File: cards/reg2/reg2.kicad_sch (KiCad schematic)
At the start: 161 parts, among them J1 BUS, Q1 2N7000, Q10 2N7000, Q11 2N7000, Q12 2N7000, Q13 2N7000, Q14 2N7000, Q15 2N7000, Q16 2N7000, Q17 2N7000, Q18 2N7000, Q19 2N7000, Q2 2N7000, Q20 2N7000, Q21 2N7000, Q22 2N7000, Q23 2N7000, Q24 2N7000, Q25 2N7000, Q26 2N7000, Q27 2N7000, Q28 2N7000, Q29 2N7000, Q3 2N7000, Q30 2N7000, Q31 2N7000, Q32 2N7000, Q33 2N7000, Q34 2N7000, Q35 2N7000, Q36 2N7000, Q37 2N7000, Q38 2N7000, Q39 2N7000, Q4 2N7000, Q40 2N7000, Q41 2N7000, Q42 2N7000, Q43 2N7000, Q44 2N7000, Q45 2N7000, Q46 2N7000, Q47 2N7000, Q48 2N7000, Q49 2N7000, Q5 2N7000, Q50 2N7000, Q51 2N7000, Q52 2N7000, Q53 2N7000, Q54 2N7000, Q55 2N7000, Q56 2N7000, Q57 2N7000, Q58 2N7000, Q59 2N7000, Q6 2N7000, Q60 2N7000, Q61 2N7000, Q62 2N7000, Q63 2N7000, Q64 2N7000, Q65 2N7000, Q66 2N7000, Q67 2N7000, Q68 2N7000, Q69 2N7000, Q7 2N7000, Q70 2N7000, Q71 2N7000, Q72 2N7000, Q73 2N7000, Q74 2N7000, Q75 2N7000, Q76 2N7000, Q77 2N7000, Q78 2N7000, Q79 2N7000, Q8 2N7000, Q80 2N7000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

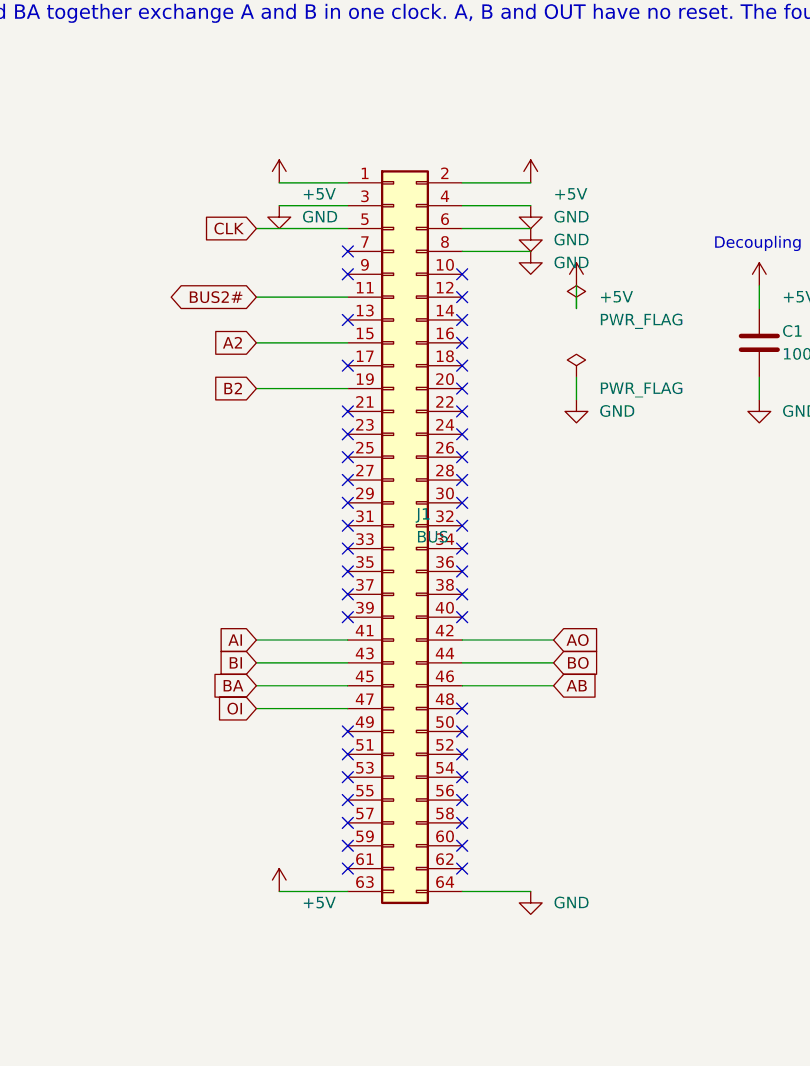
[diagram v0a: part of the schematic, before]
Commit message: The bus headers go on the back of all 26 boards, no track moved; the silkscreen refitted (D059, D062)
An IDC socket lies across its ribbon, so the ribbon could never run along a
row of cards as drawn. It runs behind them, and the 64-pin headers are
soldered on the back. This commit is that move, made in place on the routed
boards: no board was routed again.

How the header sits (D062): in the holes it had, turned over top to bottom,
notch toward the top edge. A pin of the odd row is then in the hole its even
neighbour had, so the two signals of every pair of pins change places: CLK
is pin 6, RST pin 8, +5V pins 1, 2 and 64. bus.py keeps both tables: PINS,
what the header's pins carry, and HOLES, what the copper was routed to.

The proof, on all 26 boards against 992a90f (sim/board_diff.py):
  netlist the same, element for element; every track, every via and every
  hole the same; each copper and mask layer differs by two pad shapes per
  header (pin 1's square went to the hole beside it, both on +5V) and the
  ground pour's outline round those two pads, nowhere else by more than a
  tenth of a micrometre.
sim/rebuild_check.py runs every builder into a scratch directory: each
writes the plan and the netlist that are committed, so a rebuild gives
this board. order_check.py --machine holds every pad of the 27 headers to
bus.py and requires them on the back.

What the move costs: on the ribbon RST had a ground conductor on both
sides; now one neighbour is BUS1#. tb_rst_neighbour.py puts the two lines
on the bench with every gate the routed boards hang on them: RST rises
0.28 to 0.43 V when BUS1# is released, against a lowest threshold of 0.8 V
(sim/results/rst_neighbour.md). The machine deck's crosstalk option now
couples the pins that are neighbours on the ribbon; the crosstalk stage of
the machine gate has to be run again on that order.

Silkscreen (pcb.fit_silk): every label to 1.0 mm where it has room, off
pads, vias, outlines and other labels, out from under the pa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
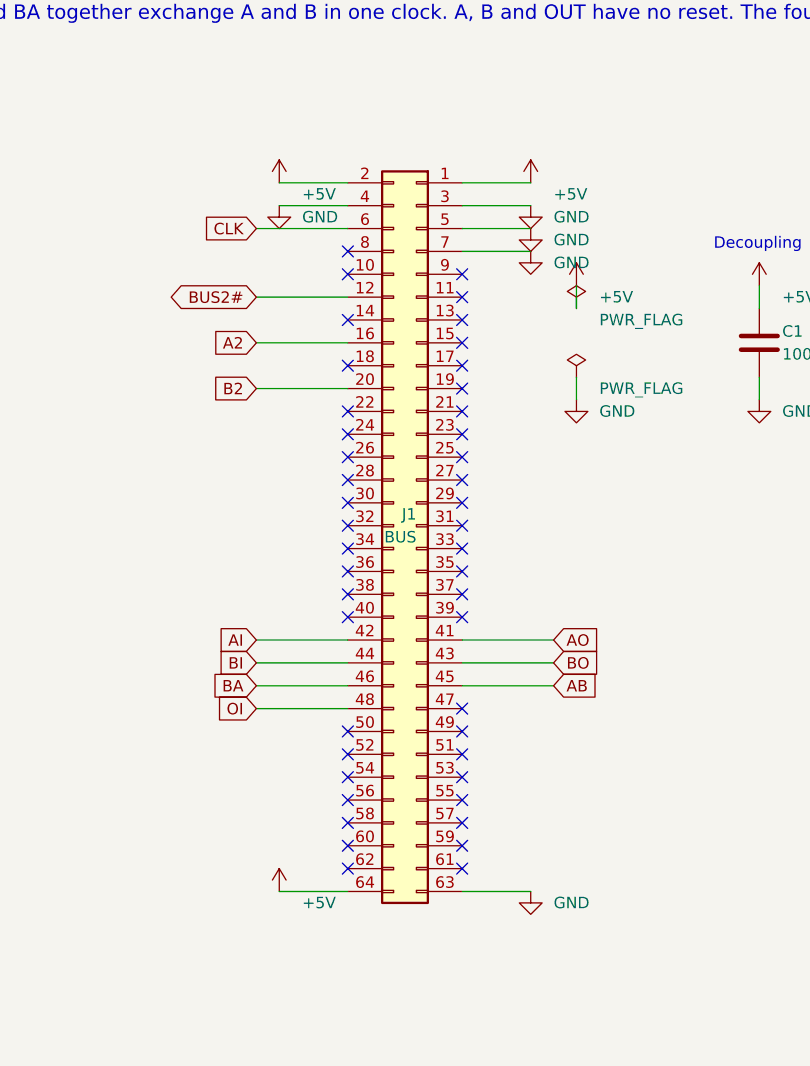
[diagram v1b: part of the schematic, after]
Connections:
- net +5V: now also J1.64 (Pin_64); no longer J1.63 (Pin_63)
- net A2: now also J1.16 (Pin_16); no longer J1.15 (Pin_15)
- net AB: now also J1.45 (Pin_45); no longer J1.46 (Pin_46)
- net AI: now also J1.42 (Pin_42); no longer J1.41 (Pin_41)
- net AO: now also J1.41 (Pin_41); no longer J1.42 (Pin_42)
- net B2: now also J1.20 (Pin_20); no longer J1.19 (Pin_19)
- net BA: now also J1.46 (Pin_46); no longer J1.45 (Pin_45)
- net BI: now also J1.44 (Pin_44); no longer J1.43 (Pin_43)
- net BO: now also J1.43 (Pin_43); no longer J1.44 (Pin_44)
- net BUS2#: now also J1.12 (Pin_12); no longer J1.11 (Pin_11)
- net CLK: now also J1.6 (Pin_6); no longer J1.5 (Pin_5)
- net GND: now also J1.5 (Pin_5), J1.63 (Pin_63), J1.7 (Pin_7); no longer J1.6 (Pin_6), J1.64 (Pin_64), J1.8 (Pin_8)
- net OI: now also J1.48 (Pin_48); no longer J1.47 (Pin_47)
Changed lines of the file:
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@@
 	(symbol
 		(lib_id "Connector_Generic:Conn_02x32_Odd_Even")
-		(at 76.2 101.6 0)
+		(at 78.74 101.6 0)
+		(mirror y)
 		(unit 1)
 		(body_style 1)
